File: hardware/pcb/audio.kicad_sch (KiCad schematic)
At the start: 0 parts

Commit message: Capture the audio sheet -- full DNP provisions
35 placements, 28 of them DNP. Only the three connectors and the two output
series resistors are fitted, which is what audio.md asks for: the capsule has
not been measured, so carbon, electret and dynamic are all laid out and the
choice becomes a population decision after the boards arrive.

All four sheets are now captured. ERC is clean at 0 violations across 125
components and 101 nets. The dangling-global count ran 33 -> 4 -> 0 as seed,
panel-io and audio landed, each drop predicted before the sheet was drawn. Five
no-connects remain and all five are deliberate: ITERM, J11 pin 9, and the three
unused 74HC14 outputs.

Verified rather than assumed, because audio.md says it is the thing that gets
forgotten: C_g sits in series with R_g, so the gain leg reaches ground through
the capacitor and DC gain is exactly 1. Without it the 1.65 V pedestal would be
amplified into the rail and the output would rest jammed at one end.

The mic return leaves on J14 instead of grounding on the sheet, so the hook
switch's second pole can break the bias current in copper rather than in
firmware. A link at J14 makes it always-on.

Each channel gets its own mid-rail divider rather than sharing one. A shared
reference would tie both non-inverting inputs together and sum the two channels.

Added a project-local MCP6002 symbol. The stock MCP6002-xSN is a derived symbol
and the embedder here refuses those; substituting the LM2904 base would have
left a misleading lib_id in the schematic for a part that is not fitted.
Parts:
- added C22, C24, C25, C26, C28, C29: 10u, Capacitor_SMD:C_0805_2012Metric, symbol Device:C
- added C23, C27: 1u, Capacitor_SMD:C_0603_1608Metric, symbol Device:C
- added C30: 100n, Capacitor_SMD:C_0603_1608Metric, symbol Device:C
- added J14: Mic bias return, Connector_JST:JST_XH_B2B-XH-A_1x02_P2.50mm_Vertical, symbol Connector_Generic:Conn_01x02
- added J17: Audio out L/R/G, Connector_JST:JST_XH_B3B-XH-A_1x03_P2.50mm_Vertical, symbol Connector_Generic:Conn_01x03
- added J18: Audio in L/R/rtn, Connector_JST:JST_XH_B3B-XH-A_1x03_P2.50mm_Vertical, symbol Connector_Generic:Conn_01x03
- added R47, R49, R58, R62: 1k, Resistor_SMD:R_0603_1608Metric, symbol Device:R
- added R48, R50, R64, R66: open, Resistor_SMD:R_0603_1608Metric, symbol Device:R
- added R51, R53: 2k2, Resistor_SMD:R_0603_1608Metric, symbol Device:R
- added R52, R54: 220R, Resistor_SMD:R_0603_1608Metric, symbol Device:R
- added R55, R56, R57, R59, R60, R61: 100k, Resistor_SMD:R_0603_1608Metric, symbol Device:R
- added R63, R65: 0R, Resistor_SMD:R_0603_1608Metric, symbol Device:R
- added U4: MCP6002, Package_SO:SOIC-8_3.9x4.9mm_P1.27mm, symbol caryatid:MCP6002
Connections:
- new net +3V3A: C30.1, R51.1, R53.1, R55.1, R59.1, U4.8 (V+)
- new net +5V: R52.1, R54.1
- new net AUDIO_IN_L: C25.2, R63.2, R64.1
- new net AUDIO_IN_R: C29.2, R65.2, R66.1
- new net AUDIO_OUT_L: R47.1
- new net AUDIO_OUT_R: R49.1
- new net GAINLEG_L: C24.1, R58.2
- new net GAINLEG_R: C28.1, R62.2
- new net GND: C22.2, C24.2, C26.2, C28.2, C30.2, J14.2 (Pin_2), J17.3 (Pin_3), R48.2, R50.2, R56.2, R60.2, R64.2, R66.2, U4.4 (V-)
- new net MIC_L: C23.1, J18.1 (Pin_1), R51.2, R52.2, R63.1
- new net MIC_R: C27.1, J18.2 (Pin_2), R53.2, R54.2, R65.1
- new net MIC_RTN: J14.1 (Pin_1), J18.3 (Pin_3)
- new net OPA_L_N: R57.1, R58.1, U4.2 (-)
- new net OPA_L_O: C25.1, R57.2, U4.1
- new net OPA_R_N: R61.1, R62.1, U4.6 (-)
- new net OPA_R_O: C29.1, R61.2, U4.7
- new net OUT_L_J: J17.1 (Pin_1), R47.2, R48.1
- new net OUT_R_J: J17.2 (Pin_2), R49.2, R50.1
- new net VBIAS_L: C22.1, C23.2, R55.2, R56.1, U4.3 (+)
- new net VBIAS_R: C26.1, C27.2, R59.2, R60.1, U4.5 (+)

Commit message: ADR 0009 step 1: jumper the mic front-end in the schematic
Three jumpers on the left channel, and the front-end populated. The PCB
is NOT yet updated -- Update PCB from Schematic, place, route and refill
zones still to do, so schematic-parity will fail until then.

  JP1  BIAS_E_L / MIC_L / BIAS_C_L      2k2 to 3V3A | off | 220R to 5V
  JP2  AMP_OUT_L / AUDIO_IN_L / BYPASS_L   op-amp | bypass
  JP3  LEG_101_L / GAINLEG_L / LEG_256_L   1k x101 | 392R x256
  R67  392R, the x256 leg, alongside R58 off OPA_L_N

SAFE TO DO BY TEXT BECAUSE THE SHEET IS LABEL-CONNECTED. Every part is a
vertical symbol with 5.08 mm pin stubs out to a named label -- confirmed
against J17 and J18, including the library-to-sheet pin transform
(sheet_x = X + lib_x, sheet_y = Y - lib_y). So inserting a jumper is a
rename plus an add, not geometric surgery.

VERIFIED BY NETLIST DIFF, WHICH IS THE REAL CHECK -- ERC does not notice
a jumper wired to the wrong net. Exactly ten nets changed, all of them
intended, and 97 of 101 pre-existing nets are byte-identical. R64
followed R63 onto BYPASS_L so the pad divider stays intact with its tap
ahead of the jumper.

Two defects caught on the way, both by ERC:

  Round coordinates (480.0, 140.0) put every pin and stub off the
  1.27 mm connection grid -- 17 endpoint_off_grid warnings. That is how
  a connection silently fails to form. All coordinates are now multiples
  of 1.27.

  JP2 stub labels were local while the labels they join were global,
  which ERC flags as same_local_global_label. Now global throughout.

ERC is 0 errors, 0 warnings.

R59/R60/R61 populated deliberately: U4 is a DUAL and populating it for
the left channel would otherwise leave section B floating, which
oscillates and draws current. With R62 left open those three make it a
unity-gain follower at VBIAS_R. Three resistors to stop an unused
amplifier misbehaving.
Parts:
- added JP1: Mic bias select, Connector_PinHeader_2.54mm:PinHeader_1x03_P2.54mm_Vertical, symbol Connector_Generic:Conn_01x03
- added JP2: Mic path select, Connector_PinHeader_2.54mm:PinHeader_1x03_P2.54mm_Vertical, symbol Connector_Generic:Conn_01x03
- added JP3: Mic gain select, Connector_PinHeader_2.54mm:PinHeader_1x03_P2.54mm_Vertical, symbol Connector_Generic:Conn_01x03
- added R67: 392R, Resistor_SMD:R_0603_1608Metric, symbol Device:R
- C22, C23, C24, C25, R51, R52, R55, R56, R57, R58, R59, R60, R61, R63, U4: now fitted
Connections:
- net AUDIO_IN_L: now also JP2.2 (Pin_2); no longer C25.2, R63.2, R64.1
- net GAINLEG_L: now also JP3.2 (Pin_2); no longer R58.2
- net MIC_L: now also JP1.2 (Pin_2); no longer R51.2, R52.2
- net OPA_L_N: now also R67.1
- new net AMP_OUT_L: C25.2, JP2.1 (Pin_1)
- new net BIAS_C_L: JP1.3 (Pin_3), R52.2
- new net BIAS_E_L: JP1.1 (Pin_1), R51.2
- new net BYPASS_L: JP2.3 (Pin_3), R63.2, R64.1
- new net LEG_101_L: JP3.1 (Pin_1), R58.2
- new net LEG_256_L: JP3.3 (Pin_3), R67.2

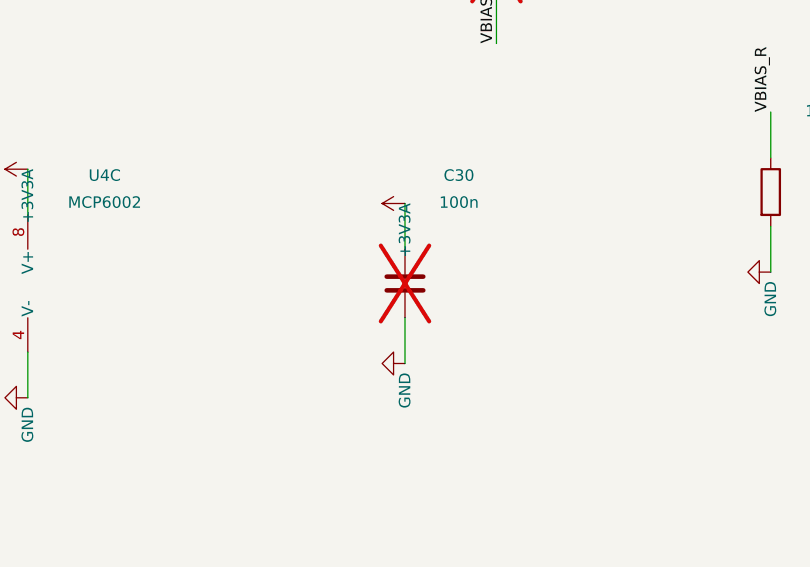
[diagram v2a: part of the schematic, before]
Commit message: Populate C30: U4 had no decoupling on +3V3A
ADR 0009 fitted U4, and left C30 -- the ONLY capacitor on +3V3A -- as
DNP. The op-amp would have been assembled with an undecoupled supply.

  +3V3A feeds  U4.8 (V+)  R51  R55  R59  J5  J9  J10
  capacitors   C30, and nothing else
  C30 was      DNP

Correctly DNP before ADR 0009: nothing active sat on that rail while U4
was unpopulated, so a decoupling cap for it was pointless. Fitting the
op-amp made it mandatory and it was not on the populate list.

CAUGHT BY TRACING WHAT THE RAIL FEEDS, NOT BY ANY CHECK. An undecoupled
supply is not a DRC violation, an ERC violation or a parity error --
eleven of eleven passed with it missing. The prompt was Matt asking why
R43 was absent from the placement preview, which is a good reason to
account for every DNP part rather than trusting the count.

ADR 0009 now records the general rule: clearing DNP on an active part
makes its support components mandatory, and they are usually DNP for the
same reason it was. Trace the supply rails after any such change.

DNP is a fabrication attribute only, so this changed no copper and
needed no zone refill.

  BOM/CPL 110 -> 111 parts, 111 of 111 sourced (C14663, already on the
  BOM for the other 100n positions -- no new part, no new loading fee)
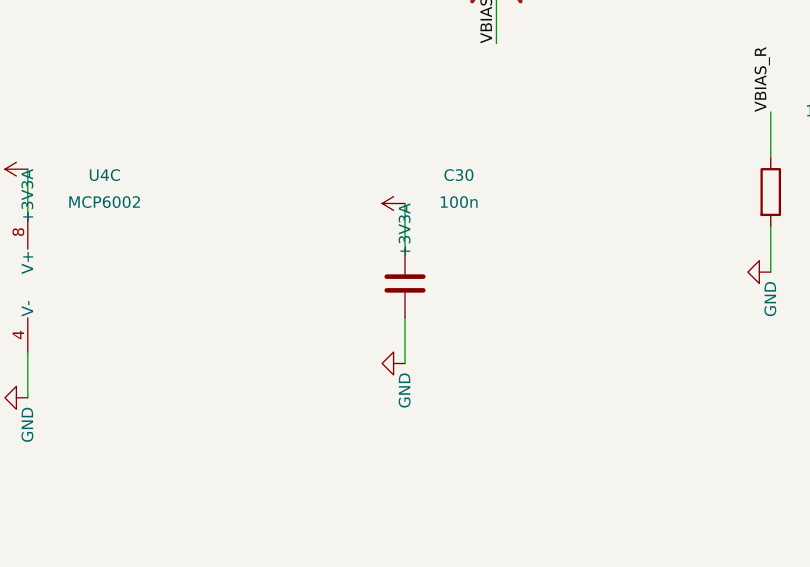
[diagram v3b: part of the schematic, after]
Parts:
- C30: now fitted
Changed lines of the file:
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@@
 		(in_bom yes)
 		(on_board yes)
-		(dnp yes)
+		(dnp no)
 		(property "Reference" "C30"
 			(at 145.7 328.36 0)

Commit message: ADR 0010 step 1: zero DNP in the schematic; the PCB is NOT yet updated
Three one-shot scripts, run in this order, and the order matters:

  drop_open_positions.py       R48 R50 R64 R66 deleted
  add_right_mic_jumpers.py     JP4/JP5/JP6 + R68, right channel assembled
  populate_panelio_options.py  R43 R44 R45 R46 assembled

R66 HAD TO GO FIRST. It taps AUDIO_IN_R at (439.42, 350.52), which is
downstream of where JP5 lands, so deleting it after the split would have
left the pad on the wrong side of the jumper. add_right_mic_jumpers.py
checks for R66 and refuses to run while it is present.

  JP4  BIAS_E_R / MIC_R / BIAS_C_R        2k2 to 3V3A | off | 220R to 5V
  JP5  AMP_OUT_R / AUDIO_IN_R / BYPASS_R  op-amp | bypass
  JP6  LEG_101_R / GAINLEG_R / LEG_256_R  1k x101 | 392R x256
  R68  392R, the x256 leg, alongside R62 off OPA_R_N

THE MIRROR IS +149.86 mm IN Y, MEASURED NOT CHOSEN. R51/R53, R58/R62,
C25/C29, R63/R65 and C24/C28 all agree, and 149.86 / 1.27 = 118, so the
translation lands every coordinate back on the connection grid. That is
the trap the left-channel run fell into first: round numbers gave 17
endpoint_off_grid warnings, and an off-grid pin is how a connection
silently fails to form.

R68 IS THE ONE PART THAT IS NOT A TRANSLATION. The left has two gain
legs, R58 1k and R67 392R; the right had only R62, because a follower
needs no second leg. Without R68 there is nothing for JP6 to select.

VERIFIED BY NETLIST DIFF, WHICH IS THE REAL CHECK -- ERC does not notice
a jumper wired to the wrong net. 99 of 107 pre-existing nets are
byte-identical, six nets are new, and every one of the eight changes is
intended:

  MIC_R       R53.2 R54.2  ->  JP4.2
  AUDIO_IN_R  C29.2 R65.2 R66.1  ->  JP5.2
  GAINLEG_R   R62.2  ->  JP6.2
  OPA_R_N     + R68.1
  OUT_L_J     - R48.1        OUT_R_J  - R50.1
  BYPASS_L    - R64.1        GND      - four shunt returns

Saved as discovery/evidence/2026-08-21-audio-netlist-diff.txt. ERC is 0
violations at --severity-all after each o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
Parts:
- removed R48, R50, R64, R66: open, Resistor_SMD:R_0603_1608Metric, symbol Device:R
- added JP4: Mic bias select R, Connector_PinHeader_2.54mm:PinHeader_1x03_P2.54mm_Vertical, symbol Connector_Generic:Conn_01x03
- added JP5: Mic path select R, Connector_PinHeader_2.54mm:PinHeader_1x03_P2.54mm_Vertical, symbol Connector_Generic:Conn_01x03
- added JP6: Mic gain select R, Connector_PinHeader_2.54mm:PinHeader_1x03_P2.54mm_Vertical, symbol Connector_Generic:Conn_01x03
- added R68: 392R, Resistor_SMD:R_0603_1608Metric, symbol Device:R
- C26, C27, C28, C29, R53, R54, R62, R65: now fitted
- JP1: value Mic bias select -> Mic bias select L
- JP2: value Mic path select -> Mic path select L
- JP3: value Mic gain select -> Mic gain select L
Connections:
- net AUDIO_IN_R: now also JP5.2 (Pin_2); no longer C29.2, R65.2
- net GAINLEG_R: now also JP6.2 (Pin_2); no longer R62.2
- net MIC_R: now also JP4.2 (Pin_2); no longer R53.2, R54.2
- net OPA_R_N: now also R68.1
- new net AMP_OUT_R: C29.2, JP5.1 (Pin_1)
- new net BIAS_C_R: JP4.3 (Pin_3), R54.2
- new net BIAS_E_R: JP4.1 (Pin_1), R53.2
- new net BYPASS_R: JP5.3 (Pin_3), R65.2
- new net LEG_101_R: JP6.1 (Pin_1), R62.2
- new net LEG_256_R: JP6.3 (Pin_3), R68.2
